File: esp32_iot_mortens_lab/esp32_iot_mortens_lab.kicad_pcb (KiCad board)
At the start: 2 copper layers, 63 parts, among them J1 Conn_01x04, J2 Screw_Terminal_01x03, J3 Screw_Terminal_01x08, J4 Screw_Terminal_01x02, J5 USB_C_Receptacle_USB2.0_16P, J6 Conn_02x05_Odd_Even, K1 RT314A05, Q1 UMH3N, Q2 BC817, SW1 SW_SPST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

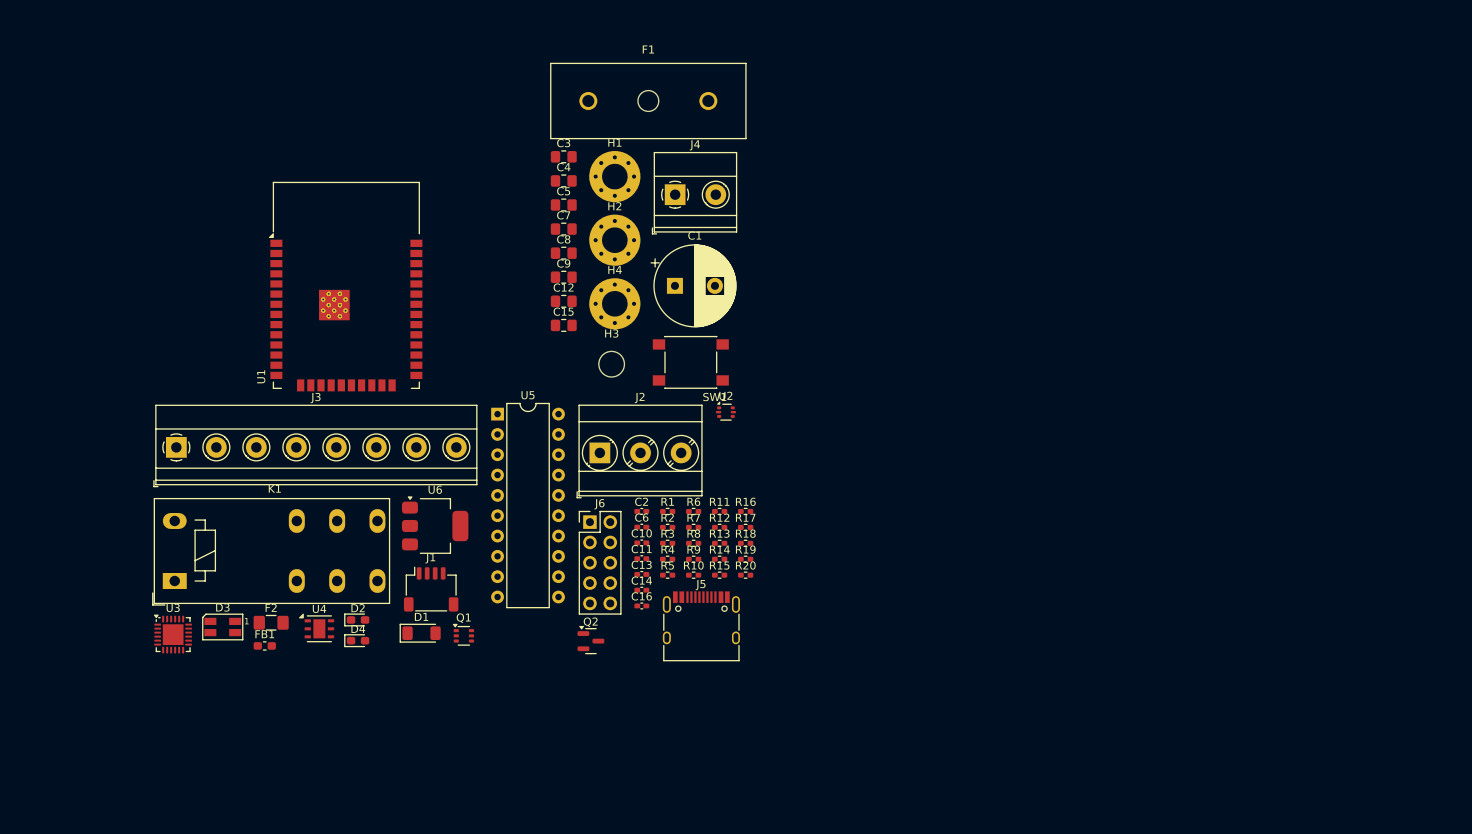
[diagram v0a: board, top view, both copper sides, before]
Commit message: pcb placement
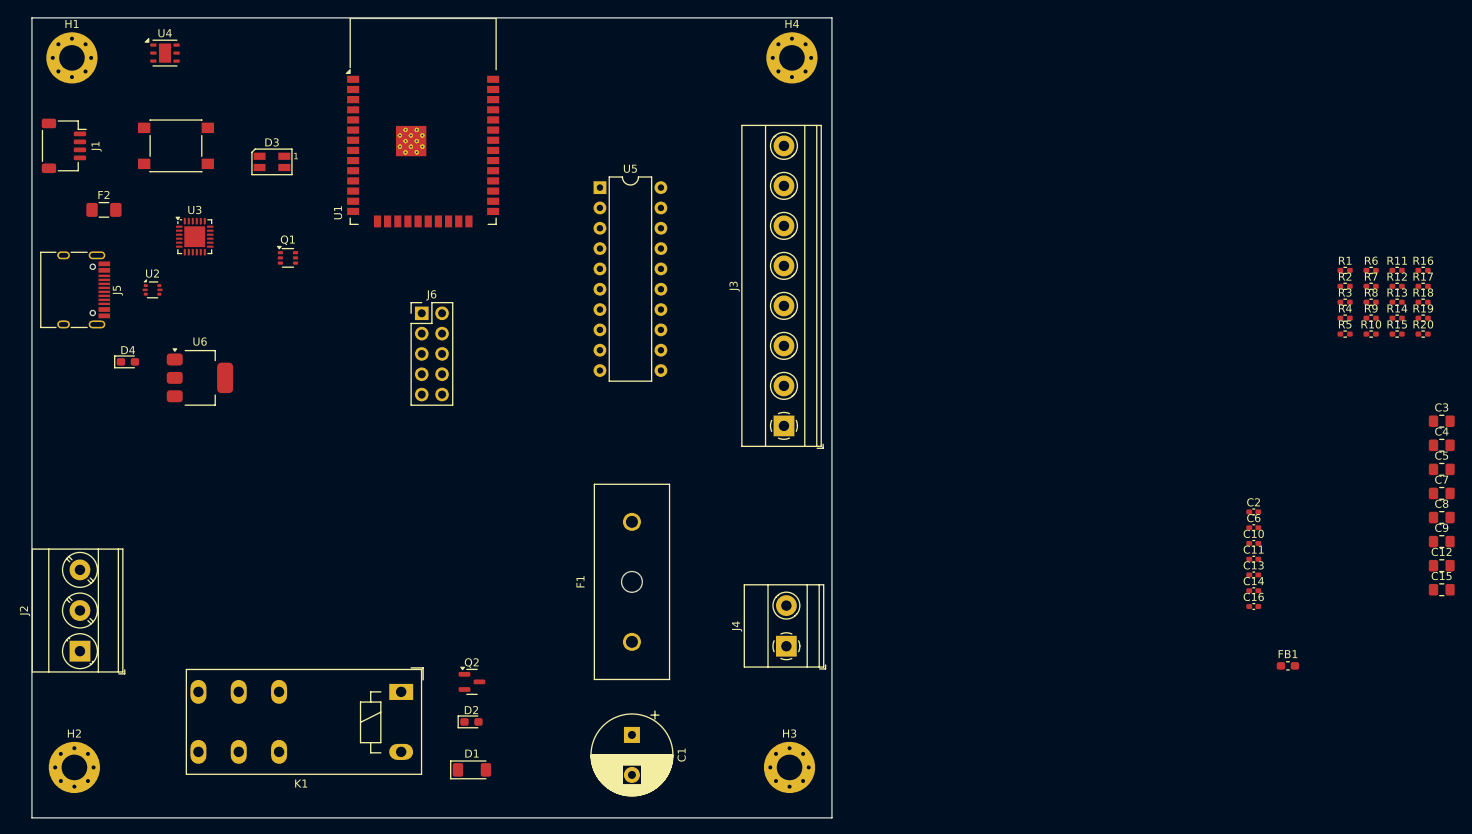
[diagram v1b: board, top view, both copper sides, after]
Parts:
- H3: footprint MountingHole:MountingHole_3.2mm_M3_DIN965 -> MountingHole:MountingHole_3.2mm_M3_Pad_Via
- moved FB1 127.9 mm to (246.0, 121.0)
- moved C12 114.6 mm to (265.2, 108.5)
- moved C15 114.6 mm to (265.2, 111.5)
- moved C3 114.6 mm to (265.2, 90.4)
- moved C4 114.6 mm to (265.2, 93.4)
- moved C5 114.6 mm to (265.2, 96.4)
- moved C7 114.6 mm to (265.2, 99.4)
- moved C8 114.6 mm to (265.2, 102.5)
- moved C9 114.6 mm to (265.2, 105.5)
- moved H2 94.4 mm to (94.3, 133.7)
- moved R1 89.9 mm to (253.2, 71.6)
- moved R2 89.9 mm to (253.2, 73.6)
- moved R3 89.9 mm to (253.2, 75.5)
- moved R4 89.9 mm to (253.2, 77.5)
- moved R5 89.9 mm to (253.2, 79.5)
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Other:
- board outline added: 100 x 100 mm
